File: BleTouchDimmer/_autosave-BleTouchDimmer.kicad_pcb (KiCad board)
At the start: 2 copper layers, 10 parts, among them SW1 SW_PUSH, U2 MDBT40, Y2 Crystal

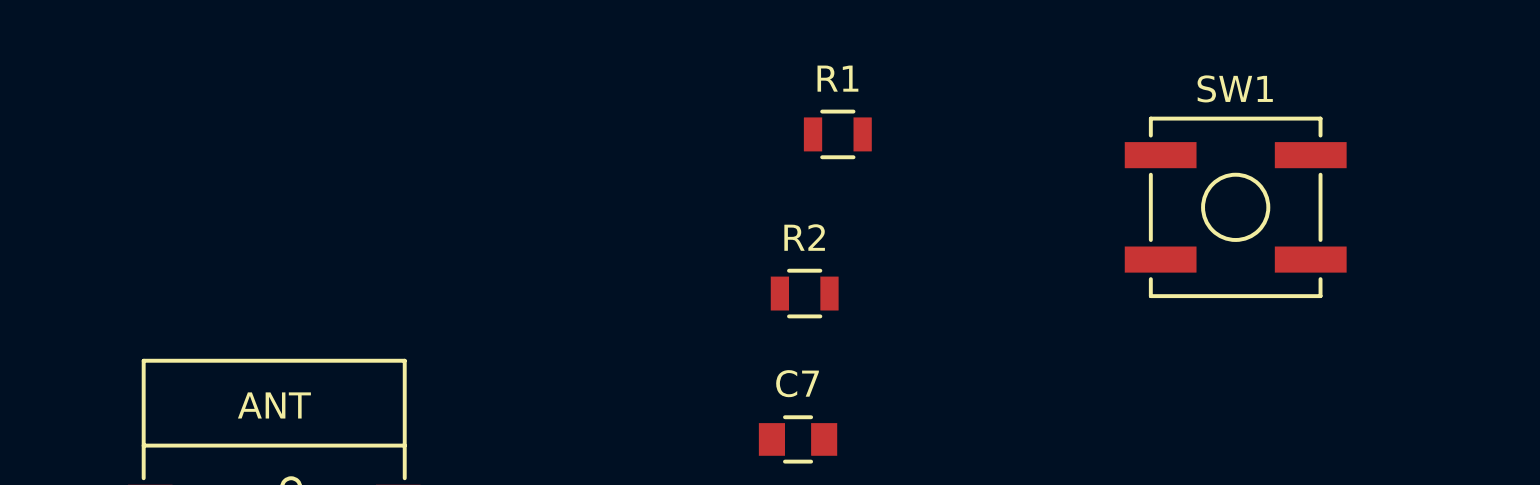
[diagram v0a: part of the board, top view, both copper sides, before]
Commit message: Added uart, reset and programming part.
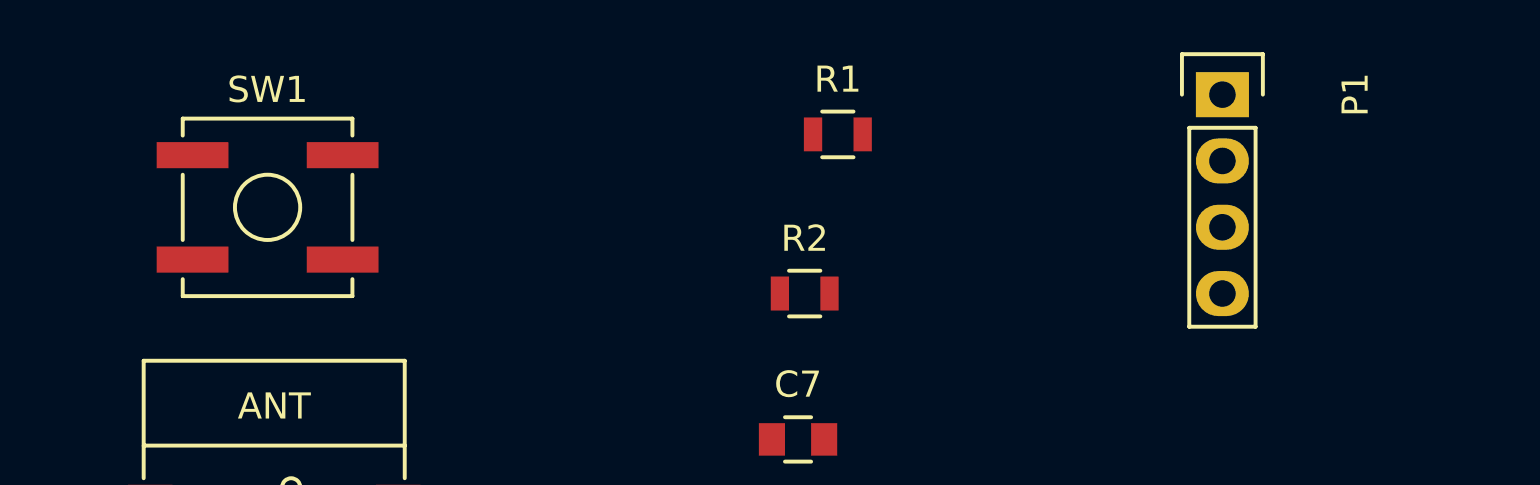
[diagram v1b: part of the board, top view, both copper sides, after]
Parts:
- added P1: CONN_01X04, Socket_Strips:Socket_Strip_Straight_1x04, F.Cu at (132.6, 60.5)
- SW1: footprint Buttons_Switches_SMD:SW_SPST_B3SL-1002P -> Buttons_Switches_SMD:SW_SPST_B3SL-1022P
- moved SW1 37.1 mm to (96.0, 64.8)
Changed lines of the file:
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@@
 (kicad_pcb (version 4) (host pcbnew 4.0.1-stable)
   (general
-    (links 25)
-    (no_connects 25)
+    (links 29)
+    (no_connects 29)
     (area 0 0 0 0)
     (thickness 1.6)
@@
     (tracks 0)
     (zones 0)
-    (modules 10)
+    (modules 11)
     (nets 7)
   )
@@
     )
   )
-  (module Buttons_Switches_SMD:SW_SPST_B3SL-1002P (layer F.Cu)
-    (at 133.096 64.77)
+  (module Buttons_Switches_SMD:SW_SPST_B3SL-1022P (layer F.Cu)
+    (at 96.012 64.77)
     (descr "Middle Stroke Tactile Switch, B3SL")
     (tags "Middle Stroke Tactile Switch")
@@
       (net 1 GND))
   )
+  (module Socket_Strips:Socket_Strip_Straight_1x04 (layer F.Cu)
+    (at 132.588 60.452 270)
+    (descr "Through hole socket strip")
+    (tags "socket strip")
+    (fp_text reference P1 (at 0 -5.1 270) (layer F.SilkS)
+      (effects (font (size 1 1) (thickness 0.15)))
+    )
+    (fp_text value CONN_01X04 (at 0 -3.1 270) (layer F.Fab)
+      (effects (font (size 1 1) (thickness 0.15)))
+    )
+    (fp_line (start -1.75 -1.75) (end -1.75 1.75) (layer F.CrtYd) (width 0.05))
+    (fp_line (start 9.4 -1.75) (end 9.4 1.75) (layer F.CrtYd) (width 0.05))
+    (fp_line (start -1.75 -1.75) (end 9.4 -1.75) (layer F.CrtYd) (width 0.05))
+    (fp_line (start -1.75 1.75) (end 9.4 1.75) (layer F.CrtYd) (width 0.05))
+    (fp_line (start 1.27 -1.27) (end 8.89 -1.27) (layer F.SilkS) (width 0.15))
+    (fp_line (start 1.27 1.27) (end 8.89 1.27) (layer F.SilkS) (width 0.15))
+    (fp_line (start -1.55 1.55) (end 0 1.55) (layer F.SilkS) (width 0.15))
+    (fp_line (start 8.89 -1.27) (end 8.89 1.27) (layer F.SilkS) (width 0.15))
+    (fp_line (start 1.27 1.27) (end 1.27 -1.27) (layer F.SilkS) (width 0.15))
+    (fp_line (start 0 -1.55) (end -1.55 -1.55) (layer F.SilkS) (width 0.15))
+    (fp_line (start -1.55 -1.55) (end -1.55 1.55) (layer F.SilkS) (width 0.15))
+    (pad 1 thru_hole rect (at 0 0 270) (size 1.7272 2.032) (drill 1.016) (layers *.Cu *.Mask)
+      (net 4 +3V3))
+    (pad 2 thru_hole oval (at 2.54 0 270) (size 1.7272 2.032) (drill 1.016) (layers *.Cu *.Mask)
+      (net 6 /SWDCLK))
+    (pad 3 thru_hole oval (at 5.08 0 270) (size 1.7272 2.032) (drill 1.016) (layers *.Cu *.Mask)
+      (net 5 /SWDIO/RESET))
+    (pad 4 thru_hole oval (at 7.62 0 270) (size 1.7272 2.032) (drill 1.016) (layers *.Cu *.Mask)
+      (net 1 GND))
+    (model Socket_Strips.3dshapes/Socket_Strip_Straight_1x04.wrl
+      (at (xyz 0.15 0 0))
+      (scale (xyz 1 1 1))
+      (rotate (xyz 0 0 180))
+    )
+  )
 )

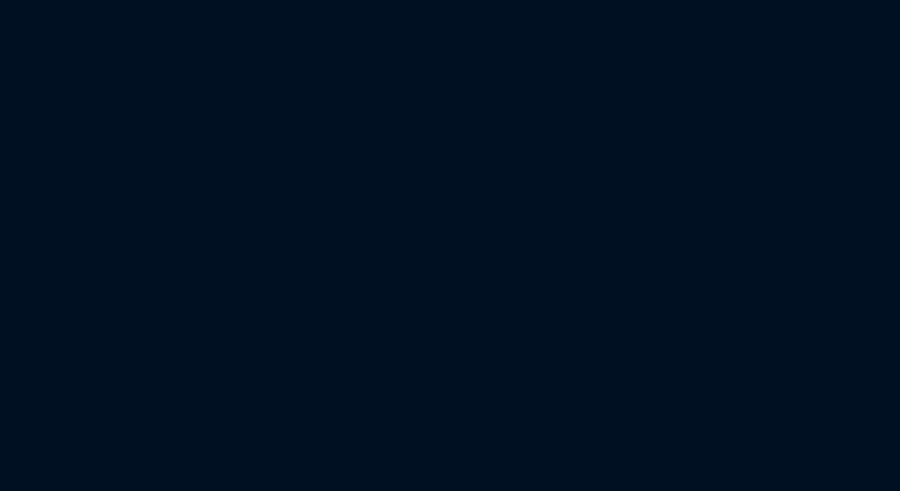
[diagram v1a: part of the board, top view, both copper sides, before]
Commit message: Updated RESET part.
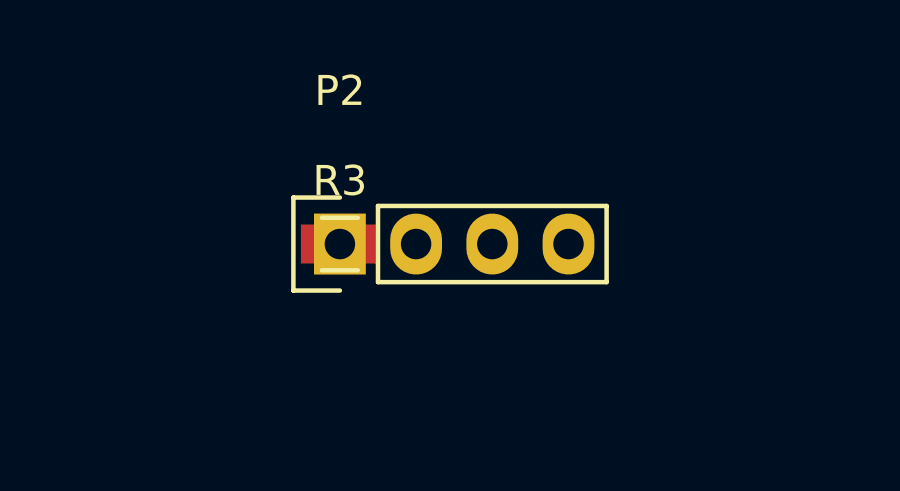
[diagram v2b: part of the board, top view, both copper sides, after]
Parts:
- added P2: UART, Socket_Strips:Socket_Strip_Straight_1x04, F.Cu at (109.2, 49.3)
- added R3: 10k, Resistors_SMD:R_0805, F.Cu at (109.2, 49.3)
- P1: value CONN_01X04 -> PROG
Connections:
- U2 pad 30: (no net) -> /RX
- U2 pad 31: (no net) -> /TX
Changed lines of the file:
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@@
 (kicad_pcb (version 4) (host pcbnew 4.0.1-stable)
   (general
-    (links 29)
-    (no_connects 29)
+    (links 35)
+    (no_connects 35)
     (area 0 0 0 0)
     (thickness 1.6)
@@
     (tracks 0)
     (zones 0)
-    (modules 11)
-    (nets 7)
+    (modules 13)
+    (nets 9)
   )
   (page A4)
@@
   (net 5 /SWDIO/RESET)
   (net 6 /SWDCLK)
+  (net 7 /RX)
+  (net 8 /TX)
   (net_class Default "This is the default net class."
     (clearance 0.2)
@@
     (uvia_drill 0.1)
     (add_net +3V3)
+    (add_net /RX)
     (add_net /SWDCLK)
     (add_net /SWDIO/RESET)
+    (add_net /TX)
     (add_net GND)
     (add_net "Net-(C3-Pad2)")
@@
     (pad 28 smd rect (at 4.75 -3.2) (size 1.7 0.5) (layers F.Cu F.Paste F.Mask))
     (pad 29 smd rect (at 4.75 -3.9) (size 1.7 0.5) (layers F.Cu F.Paste F.Mask))
-    (pad 30 smd rect (at 4.75 -4.6) (size 1.7 0.5) (layers F.Cu F.Paste F.Mask))
-    (pad 31 smd rect (at 4.75 -5.3) (size 1.7 0.5) (layers F.Cu F.Paste F.Mask))
+    (pad 30 smd rect (at 4.75 -4.6) (size 1.7 0.5) (layers F.Cu F.Paste F.Mask)
+      (net 7 /RX))
+    (pad 31 smd rect (at 4.75 -5.3) (size 1.7 0.5) (layers F.Cu F.Paste F.Mask)
+      (net 8 /TX))
     (pad 32 smd rect (at 4.75 -6) (size 1.7 0.5) (layers F.Cu F.Paste F.Mask))
     (pad 33 smd rect (at 4.75 -6.7) (size 1.7 0.5) (layers F.Cu F.Paste F.Mask))
@@
       (effects (font (size 1 1) (thickness 0.15)))
     )
-    (fp_text value CONN_01X04 (at 0 -3.1 270) (layer F.Fab)
+    (fp_text value PROG (at 0 -3.1 270) (layer F.Fab)
       (effects (font (size 1 1) (thickness 0.15)))
     )
@@
     )
   )
+  (module Socket_Strips:Socket_Strip_Straight_1x04 (layer F.Cu)
+    (at 109.22 49.276)
+    (descr "Through hole socket strip")
+    (tags "socket strip")
+    (fp_text reference P2 (at 0 -5.1) (layer F.SilkS)
+      (effects (font (size 1 1) (thickness 0.15)))
+    )
+    (fp_text value UART (at 0 -3.1) (layer F.Fab)
+      (effects (font (size 1 1) (thickness 0.15)))
+    )
+    (fp_line (start -1.75 -1.75) (end -1.75 1.75) (layer F.CrtYd) (width 0.05))
+    (fp_line (start 9.4 -1.75) (end 9.4 1.75) (layer F.CrtYd) (width 0.05))
+    (fp_line (start -1.75 -1.75) (end 9.4 -1.75) (layer F.CrtYd) (width 0.05))
+    (fp_line (start -1.75 1.75) (end 9.4 1.75) (layer F.CrtYd) (width 0.05))
+    (fp_line (start 1.27 -1.27) (end 8.89 -1.27) (layer F.SilkS) (width 0.15))
+    (fp_line (start 1.27 1.27) (end 8.89 1.27) (layer F.SilkS) (width 0.15))
+    (fp_line (start -1.55 1.55) (end 0 1.55) (layer F.SilkS) (width 0.15))
+    (fp_line (start 8.89 -1.27) (end 8.89 1.27) (layer F.SilkS) (width 0.15))
+    (fp_line (start 1.27 1.27) (end 1.27 -1.27) (layer F.SilkS) (width 0.15))
+    (fp_line (start 0 -1.55) (end -1.55 -1.55) (layer F.SilkS) (width 0.15))
+    (fp_line (start -1.55 -1.55) (end -1.55 1.55) (layer F.SilkS) (width 0.15))
+    (pad 1 thru_hole rect (at 0 0) (size 1.7272 2.032) (drill 1.016) (layers *.Cu *.Mask)
+      (net 4 +3V3))
+    (pad 2 thru_hole oval (at 2.54 0) (size 1.7272 2.032) (drill 1.016) (layers *.Cu *.Mask)
+      (net 7 /RX))
+    (pad 3 thru_hole oval (at 5.08 0) (size 1.7272 2.032) (drill 1.016) (layers *.Cu *.Mask)
+      (net 8 /TX))
+    (pad 4 thru_hole oval (at 7.62 0) (size 1.7272 2.032) (drill 1.016) (layers *.Cu *.Mask)
+      (net 1 GND))
+    (model Socket_Strips.3dshapes/Socket_Strip_Straight_1x04.wrl
+      (at (xyz 0.15 0 0))
+      (scale (xyz 1 1 1))
+      (rotate (xyz 0 0 180))
+    )
+  )
+  (module Resistors_SMD:R_0805 (layer F.Cu)
+    (at 109.22 49.276)
+    (descr "Resistor SMD 0805, reflow soldering, Vishay (see dcrcw.pdf)")
+    (tags "resistor 0805")
+    (attr smd)
+    (fp_text reference R3 (at 0 -2.1) (layer F.SilkS)
+      (effects (font (size 1 1) (thickness 0.15)))
+    )
+    (fp_text value 10k (at 0 2.1) (layer F.Fab)
+      (effects (font (size 1 1) (thickness 0.15)))
+    )
+    (fp_line (start -1.6 -1) (end 1.6 -1) (layer F.CrtYd) (width 0.05))
+    (fp_line (start -1.6 1) (end 1.6 1) (layer F.CrtYd) (width 0.05))
+    (fp_line (start -1.6 -1) (end -1.6 1) (layer F.CrtYd) (width 0.05))
+    (fp_line (start 1.6 -1) (end 1.6 1) (layer F.CrtYd) (width 0.05))
+    (fp_line (start 0.6 0.875) (end -0.6 0.875) (layer F.SilkS) (width 0.15))
+    (fp_line (start -0.6 -0.875) (end 0.6 -0.875) (layer F.SilkS) (width 0.15))
+    (pad 1 smd rect (at -0.95 0) (size 0.7 1.3) (layers F.Cu F.Paste F.Mask)
+      (net 7 /RX))
+    (pad 2 smd rect (at 0.95 0) (size 0.7 1.3) (layers F.Cu F.Paste F.Mask)
+      (net 4 +3V3))
+    (model Resistors_SMD.3dshapes/R_0805.wrl
+      (at (xyz 0 0 0))
+      (scale (xyz 1 1 1))
+      (rotate (xyz 0 0 0))
+    )
+  )
